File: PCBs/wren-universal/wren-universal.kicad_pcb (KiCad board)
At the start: 2 copper layers, 227.7 x 112.8 mm, 117 parts, among them J1 TRRS_Jack, SW0 Reset, U1 Elite-C

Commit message: Add Egg detachable macro pad
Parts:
- added H8: MountingHole, MountingHole:MountingHole_5.5mm, F.Cu at (94.4, 65.1)
- added H9: MountingHole, MountingHole:MountingHole_5.5mm, F.Cu at (56.3, 65.1)
- added U2: EGG PRO MICRO, footprints:ARDUINO_PRO_MICRO, B.Cu at (104.0, 42.9)
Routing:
- net ROW3: track 291.3 -> 335.7 mm, vias 0 -> 1
- net ROW2: track 243.0 -> 269.9 mm, vias 0 -> 1
- net COL7: track 231.9 -> 246.6 mm
- net ROW1: track 265.8 -> 278.5 mm
- net COL6: track 211.9 -> 223.5 mm
- net COL9: track 282.3 -> 287.8 mm, vias 4 -> 5
- net COL8: track 269.8 -> 273.6 mm
- net ROW0: track 221.7 -> 223.1 mm
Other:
- outline, holes or cut-outs redrawn

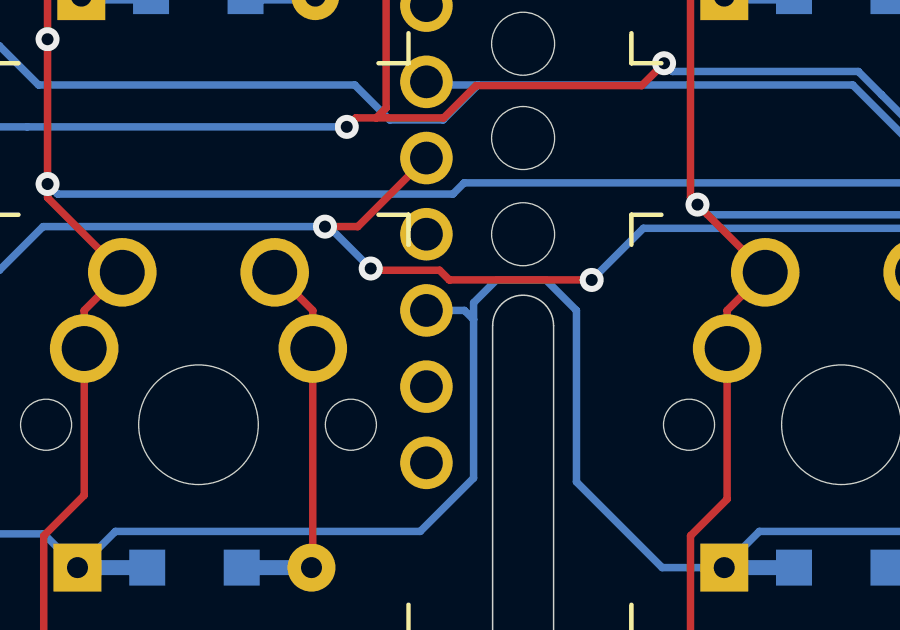
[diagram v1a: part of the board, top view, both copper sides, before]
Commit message: Update readme for Egg
Update readme to add references to the Egg macropad, as well as add Egg plate Gerbers
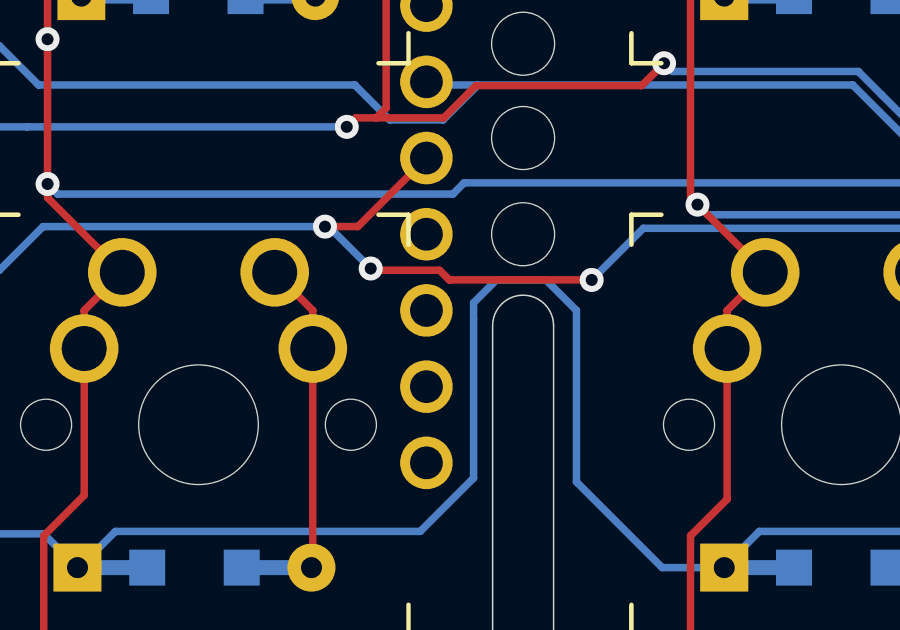
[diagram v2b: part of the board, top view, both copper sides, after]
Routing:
- net ROW1: track 278.5 -> 276.8 mm

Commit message: Minor Changes
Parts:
- moved D13 26.6 mm to (184.5, 78.1)
- moved D2 26.6 mm to (203.5, 61.5)
- moved D21 26.6 mm to (222.6, 101.9)
- moved D23 26.6 mm to (184.5, 97.2)
- moved D25 26.6 mm to (146.4, 105.9)
- moved D26 26.6 mm to (127.3, 105.9)
- moved D27 26.6 mm to (105.9, 105.9)
- moved D28 26.6 mm to (86.8, 105.9)
- moved D29 26.6 mm to (67.8, 105.9)
- moved D30 26.6 mm to (48.7, 105.9)
- moved D31 26.6 mm to (222.6, 121.0)
- moved D33 26.6 mm to (184.5, 116.2)
- moved D35 26.6 mm to (146.4, 125.0)
- moved D36 26.6 mm to (127.3, 125.0)
- moved D37 26.6 mm to (105.9, 125.0)
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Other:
- outline, holes or cut-outs redrawn

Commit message: Clean up design rules, traces.
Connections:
- U1 pad 3: GND -> (no net)
- U1 pad 4: GND -> (no net)
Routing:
- net ROW4: track 157.6 -> 179.1 mm
- net SDA: track 82.7 -> 82.1 mm
